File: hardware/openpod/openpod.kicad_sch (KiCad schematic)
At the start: 3 parts

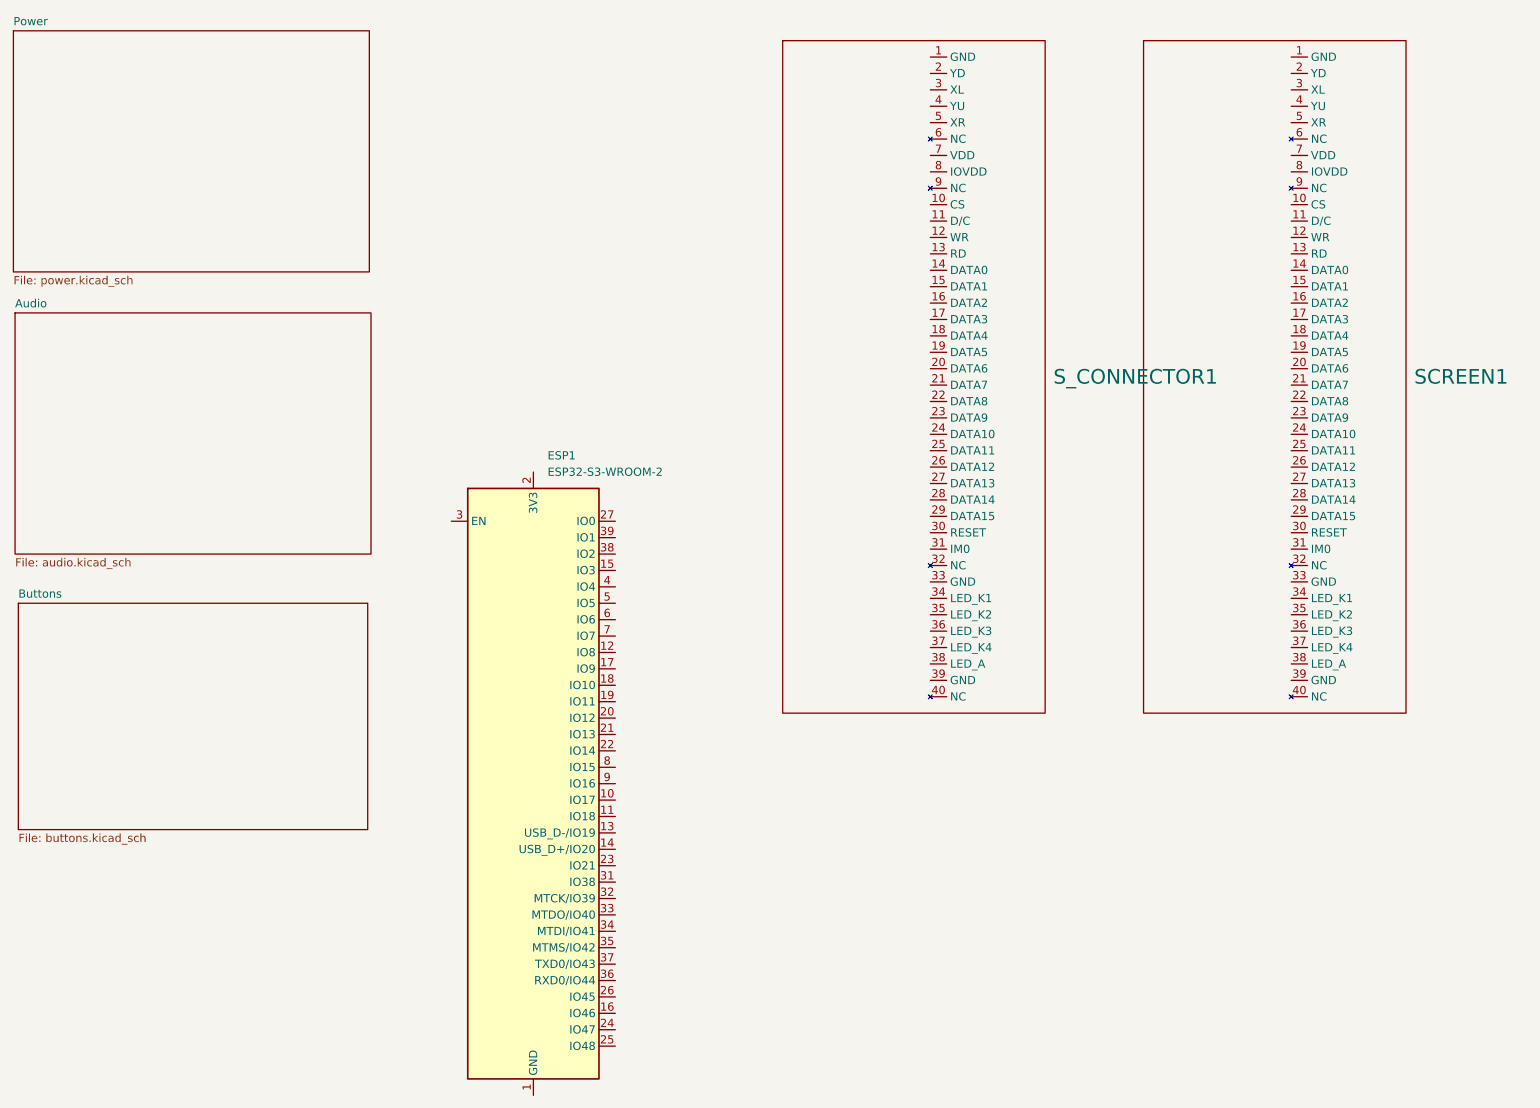
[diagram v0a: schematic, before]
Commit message: Rebirth (#2)
* designed clickwheel and see if mpr121 can fit on it

* update power and audio

* added UART converter

* added bluetooth

* try up with vs1053 feather

* setupt the player file

* fill screen with different colors

* almost works with GFX, just wrong coordinates

* test MADCTL 1

* wrong, screen is all white

* screen pins before remap

* new pinout with consecutive 16bits on the PCs pins

* screen works

* added demo

* updated platformio.ini

* added blog

* cleanup

* first menu

* Fast (ugly) menu renderer

* ugly theme + blog post

* transition using HW scrolling

* breakdown ui

* 30 rows buffer

* remove row/col shit

* added content for the blog

* start restoring render of the now playing

* scroll to nowplaying

* working transitiontotracklist (but slight prolbem with last line)

* fixed the wrapping issue at the bottom

* update theme

* rewired vs1053

* screen and mp3 working

* pins

* updated mp3 pinout to have i2c available

* testing the clickwheel with teleplot: looking good !

* Debugging the wheel: it follows my finger on the screen

* first scrolling the tracks with the wheel !

* WIP

* use an app state and allow to use more bits per pixel

* setup unit tests

* std

* remove select track

* use doctest and reporter

* make tests pass

* cleanup

* fixed scripts

* faster render fonts

* dark background

* better state + events handler system

* wip

* faster renderer of tracklist + animations + better split between concerns

* 2 bits per pixel

* docs

* remove unit tests

* simplify ui list

* rename track to element

* rename track to element

* psram controller

* psram works on SPI1

* psram controller works

* indexer

* crawler

* radix tree?

* update trie generator

* started implementing storage

* trie index

* search works on the stm32

* can retrieve now paths

* sound player on the way

* enhanced mp3 working, but not flac

* flac plugin

* config files

* load flac plugin correctly: saccaded sound

* cleaning up

*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
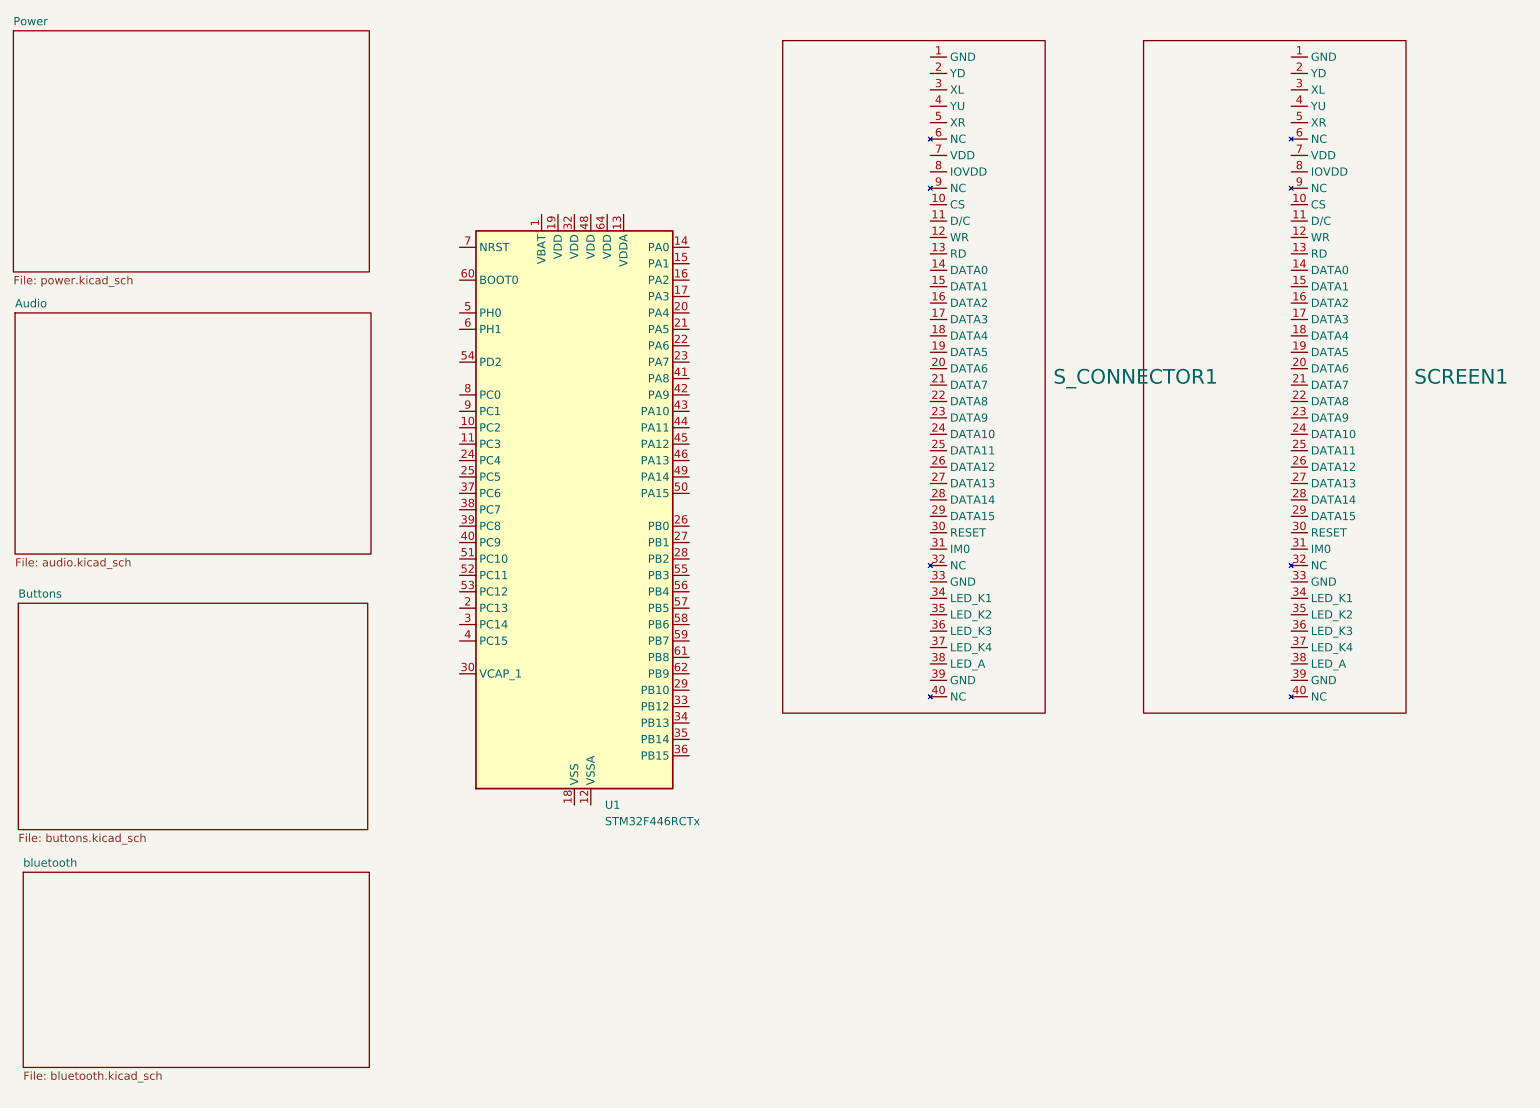
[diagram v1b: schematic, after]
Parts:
- removed ESP1: ESP32-S3-WROOM-2, openpod:ESP32-S3-WROOM-2, symbol RF_Module:ESP32-S3-WROOM-2
- added U1: STM32F446RCTx, Package_QFP:LQFP-64_10x10mm_P0.5mm, symbol MCU_ST_STM32F4:STM32F446RCTx
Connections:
- new net: U1.18 (VSS), U1.31 (VSS), U1.47 (VSS), U1.63 (VSS)
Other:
- added sheet bluetooth (bluetooth.kicad_sch)
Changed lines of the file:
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@@
 (kicad_sch (version 20230121) (generator eeschema)
   (paper "A4")
-  (symbol (lib_id "RF_Module:ESP32-S3-WROOM-2") (at 148.082 140.462 0) (unit 1)
+  (symbol (lib_id "MCU_ST_STM32F4:STM32F446RCTx") (at 154.432 98.044 0) (unit 1)
     (in_bom yes) (on_board yes) (dnp no) (fields_autoplaced)
-    (property "Reference" "ESP1" (at 150.2761 89.662 0)
+    (property "Reference" "U1" (at 159.1661 143.764 0)
       (effects (font (size 1.27 1.27)) (justify left))
     )
-    (property "Value" "ESP32-S3-WROOM-2" (at 150.2761 92.202 0)
+    (property "Value" "STM32F446RCTx" (at 159.1661 146.304 0)
       (effects (font (size 1.27 1.27)) (justify left))
     )
-    (property "Footprint" "openpod:ESP32-S3-WROOM-2" (at 148.082 201.422 0)
-      (effects (font (size 1.27 1.27)) hide)
-    )
-    (property "Datasheet" "https://www.espressif.com/sites/default/files/documentation/esp32-s3-wroom-2_datasheet_en.pdf" (at 148.082 203.962 0)
-      (effects (font (size 1.27 1.27)) hide)
-    )
-    (property "Manufacturer" "Espressif Systems" (at 148.082 140.462 0)
-      (effects (font (size 1.27 1.27)) hide)
-    )
-    (property "Part number" "ESP32-S3-WROOM-2-N32R16V" (at 148.082 140.462 0)
-      (effects (font (size 1.27 1.27)) hide)
-    )
-    (property "Supplier" "DigiKey" (at 148.082 140.462 0)
-      (effects (font (size 1.27 1.27)) hide)
-    )
-    (property "Supplier Part number" "1965-ESP32-S3-WROOM-2-N32R16VTR-ND" (at 148.082 140.462 0)
-      (effects (font (size 1.27 1.27)) hide)
-    )
+    (property "Footprint" "Package_QFP:LQFP-64_10x10mm_P0.5mm" (at 139.192 141.224 0)
+      (effects (font (size 1.27 1.27)) (justify right) hide)
+    )
+    (property "Datasheet" "https://www.st.com/resource/en/datasheet/stm32f446rc.pdf" (at 154.432 98.044 0)
+      (effects (font (size 1.27 1.27)) hide)
+    )
+    (property "Manufacturer" "STMicroelectronics" (at 154.432 98.044 0)
+      (effects (font (size 1.27 1.27)) hide)
+    )
+    (property "Part number" "STM32F446RCT6TR" (at 154.432 98.044 0)
+      (effects (font (size 1.27 1.27)) hide)
+    )
+    (property "Supplier" "DigiKey" (at 154.432 98.044 0)
+      (effects (font (size 1.27 1.27)) hide)
+    )
+    (property "Supplier Part number" "497-19357-2-ND" (at 154.432 98.044 0)
+      (effects (font (size 1.27 1.27)) hide)
+    )
+    (pin "54")
+    (pin "5")
+    (pin "47")
+    (pin "8")
+    (pin "42")
+    (pin "48")
+    (pin "56")
+    (pin "23")
+    (pin "9")
+    (pin "53")
+    (pin "31")
+    (pin "4")
+    (pin "49")
+    (pin "63")
+    (pin "16")
+    (pin "50")
+    (pin "29")
+    (pin "30")
+    (pin "46")
+    (pin "27")
+    (pin "26")
+    (pin "62")
+    (pin "24")
+    (pin "13")
+    (pin "64")
+    (pin "20")
+    (pin "34")
+    (pin "44")
+    (pin "41")
+    (pin "40")
+    (pin "51")
+    (pin "37")
+    (pin "25")
+    (pin "60")
+    (pin "55")
+    (pin "61")
+    (pin "6")
+    (pin "43")
+    (pin "45")
+    (pin "28")
+    (pin "3")
+    (pin "52")
+    (pin "7")
     (pin "39")
+    (pin "38")
+    (pin "33")
+    (pin "36")
     (pin "17")
-    (pin "40")
-    (pin "4")
-    (pin "31")
-    (pin "41")
-    (pin "8")
+    (pin "21")
+    (pin "32")
+    (pin "19")
+    (pin "58")
+    (pin "11")
+    (pin "35")
+    (pin "2")
+    (pin "22")
+    (pin "18")
+    (pin "57")
+    (pin "59")
+    (pin "12")
+    (pin "14")
     (pin "15")
-    (pin "14")
     (pin "10")
-    (pin "11")
-    (pin "21")
-    (pin "20")
-    (pin "18")
-    (pin "36")
-    (pin "33")
-    (pin "35")
-    (pin "13")
-    (pin "3")
-    (pin "6")
-    (pin "27")
-    (pin "29")
-    (pin "25")
-    (pin "28")
-    (pin "26")
-    (pin "23")
-    (pin "24")
-    (pin "22")
-    (pin "9")
-    (pin "19")
-    (pin "34")
-    (pin "2")
-    (pin "38")
-    (pin "5")
     (pin "1")
-    (pin "12")
-    (pin "16")
-    (pin "30")
-    (pin "32")
-    (pin "7")
-    (pin "37")
     (instances
       (project "openpod"
         (path "/0122bb8c-dbef-4db1-a6c6-9be780a38d9f"
-          (reference "ESP1") (unit 1)
+          (reference "U1") (unit 1)
         )
       )
@@
       )
     )
+  )
+  (sheet (at 69.088 154.178) (size 53.594 30.226) (fields_autoplaced)
+    (stroke (width 0.1524) (type solid))
+    (fill (color 0 0 0 0.0000))
+    (property "Sheetname" "bluetooth" (at 69.088 153.4664 0)
+      (effects (font (size 1.27 1.27)) (justify left bottom))
+    )
+    (property "Sheetfile" "bluetooth.kicad_sch" (at 69.088 184.9886 0)
+      (effects (font (size 1.27 1.27)) (justify left top))
+    )
+    (instances
+      (project "openpod"
+        (path "/0122bb8c-dbef-4db1-a6c6-9be780a38d9f" (page "5"))
+      )
+    )
